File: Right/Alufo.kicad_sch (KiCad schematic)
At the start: 23 parts, among them J2 USB_C_Receptacle_USB2.0_16P_2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, J4 USB_C_Receptacle_USB2.0_16P_2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, SW2 BOOT, U2 CH552T, U4 USBLC6-2P6, U6 USBLC6-2P6

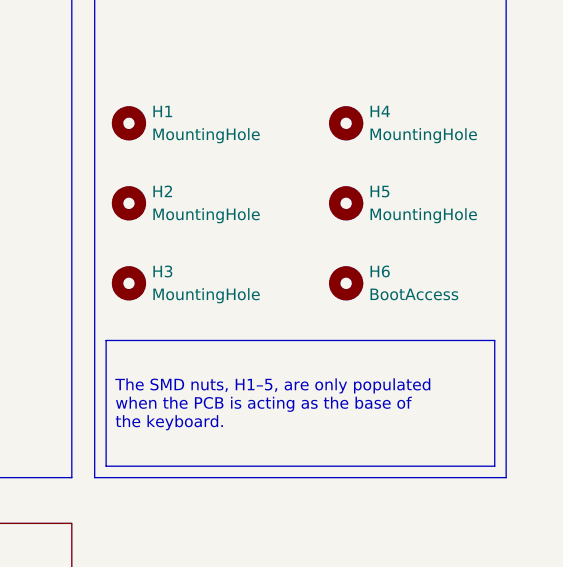
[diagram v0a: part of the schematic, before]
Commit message: Revert boot access hole change
It was correct before!
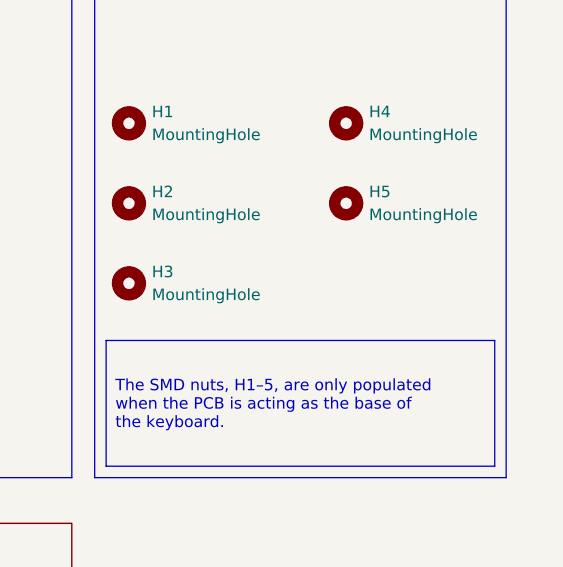
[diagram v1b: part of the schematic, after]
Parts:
- removed H6: BootAccess, MountingHole:MountingHole_2.5mm, symbol Mechanical:MountingHole
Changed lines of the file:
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@@
-	)
-	(symbol
-		(lib_id "Mechanical:MountingHole")
-		(at 177.8 176.53 0)
-		(unit 1)
-		(exclude_from_sim yes)
-		(in_bom no)
-		(on_board yes)
-		(dnp no)
-		(fields_autoplaced yes)
-		(property "Reference" "H6"
-			(at 180.34 175.2599 0)
-			(effects
-				(font
-					(size 1.27 1.27)
-				)
-				(justify left)
-			)
-		)
-		(property "Value" "BootAccess"
-			(at 180.34 177.7999 0)
-			(effects
-				(font
-					(size 1.27 1.27)
-				)
-				(justify left)
-			)
-		)
-		(property "Footprint" "MountingHole:MountingHole_2.5mm"
-			(at 177.8 176.53 0)
-			(effects
-				(font
-					(size 1.27 1.27)
-				)
-				(hide yes)
-			)
-		)
-		(property "Datasheet" "~"
-			(at 177.8 176.53 0)
-			(effects
-				(font
-					(size 1.27 1.27)
-				)
-				(hide yes)
-			)
-		)
-		(property "Description" "Mounting Hole without connection"
-			(at 177.8 176.53 0)
-			(effects
-				(font
-					(size 1.27 1.27)
-				)
-				(hide yes)
-			)
-		)
-		(instances
-			(project "Alufo"
-				(path "/52f043ac-ccff-4c85-bc10-2db9d3c9e3f3"
-					(reference "H6")
-					(unit 1)
-				)
-			)
-		)
 	)
 	(symbol

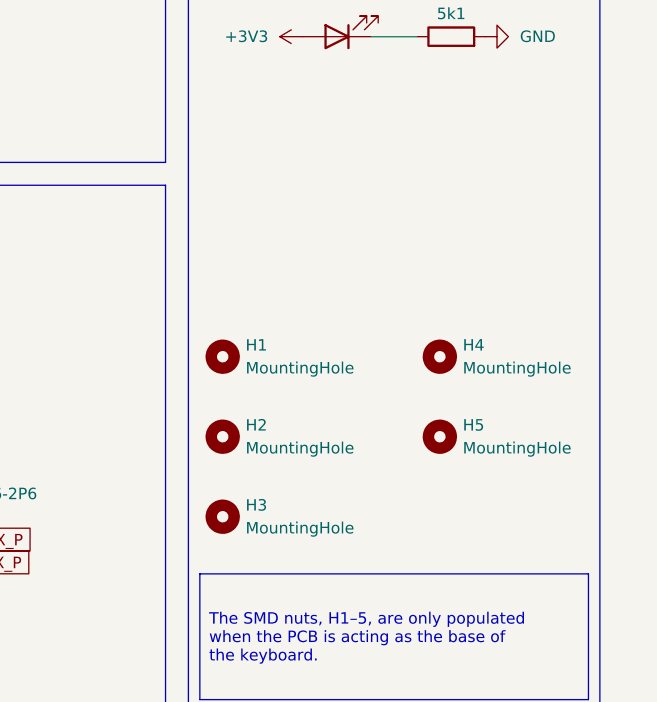
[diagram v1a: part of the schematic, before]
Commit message: Add plate to righthand board
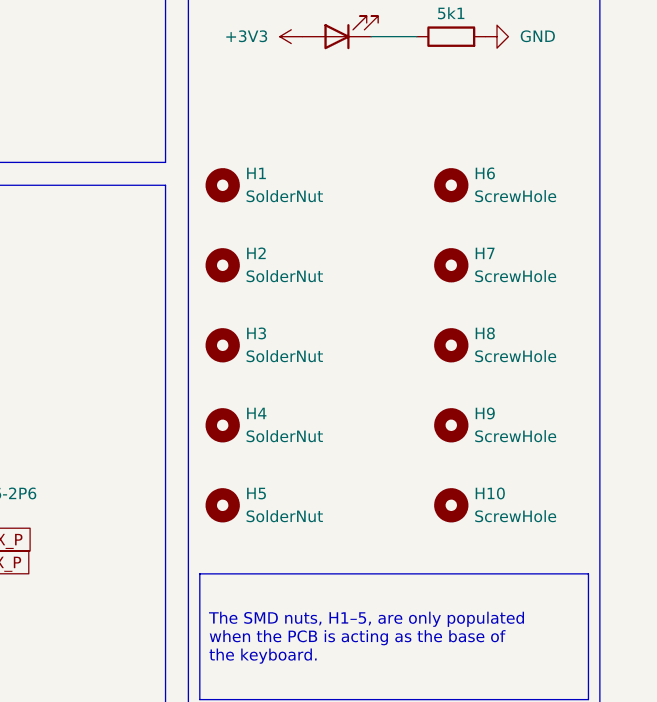
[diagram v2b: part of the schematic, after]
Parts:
- added H10, H6, H7, H8, H9: ScrewHole, MountingHole:MountingHole_2.2mm_M2, symbol Mechanical:MountingHole
- H1, H2, H3, H4, H5: value MountingHole -> SolderNut

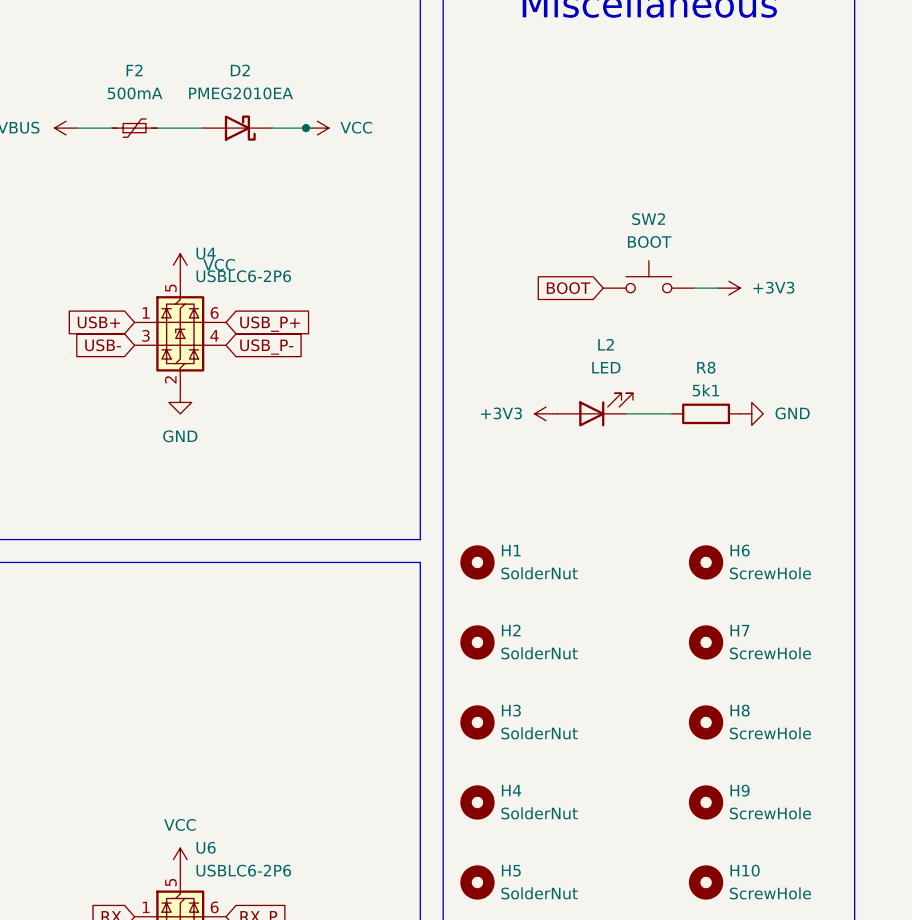
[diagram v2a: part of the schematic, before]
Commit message: Connect aluminium back to copper layer
Holes J5 and J6 will be filled with solder on the active PCB to connect the back aluminium layer (which is connected to the USB shield) with the mounting hole H3. H3 will in turn connect to the bottom layer PCB via the solder nut pressed against the exposed pad on the active PCB. The solder nut will connect to the screw and the screw will connect to the top plate. The upper middle plate will connect to the shield by virtue of being physically pressed to the active PCB’s back (if correctly oriented).
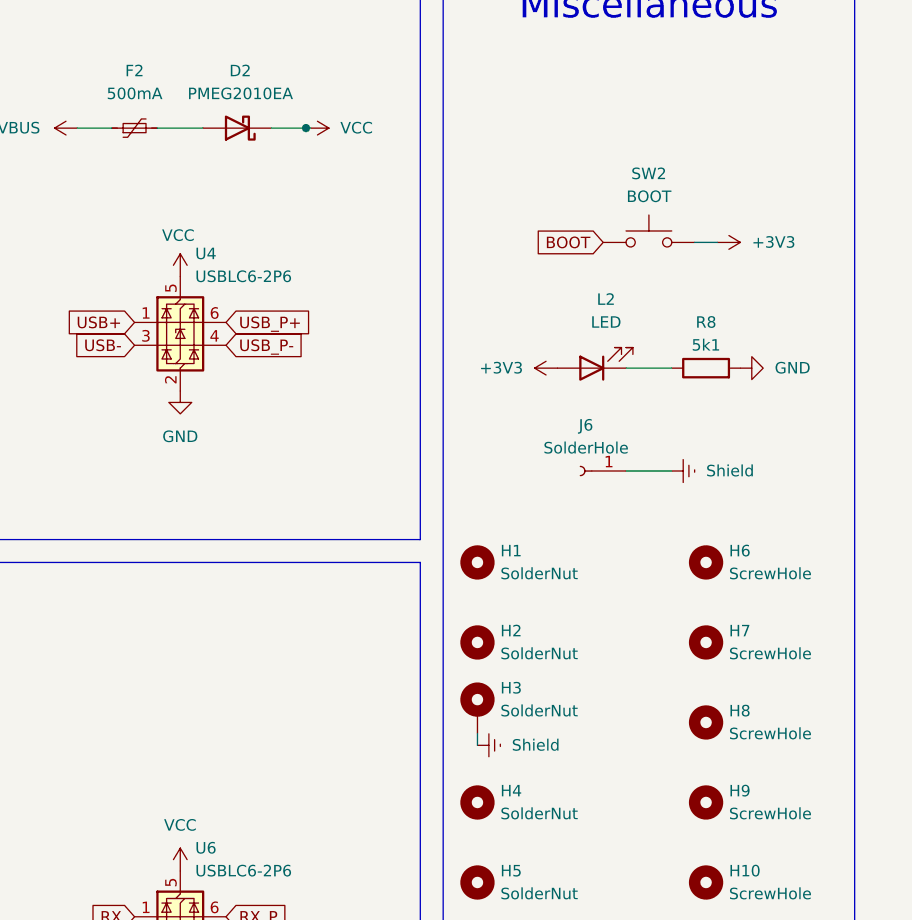
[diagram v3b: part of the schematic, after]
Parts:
- added J6: SolderHole, TestPoint:TestPoint_THTPad_D2.5mm_Drill1.2mm, symbol Connector:Conn_01x01_Socket
- H3: footprint Project Library:MountingHole_2.2mm_M2_SMD_Solder_Nut -> Project Library:MountingHole_2.2mm_M2_SMD_Solder_Nut_Pad; symbol Mechanical:MountingHole -> Mechanical:MountingHole_Pad
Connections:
- new net Shield: H3.1, J6.1 (Pin_1)
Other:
- moved on the sheet: L2, R8, SW2

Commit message: Do not exclude solder nuts from BOM
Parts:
- H1, H2, H3, H4, H5: now in the parts list

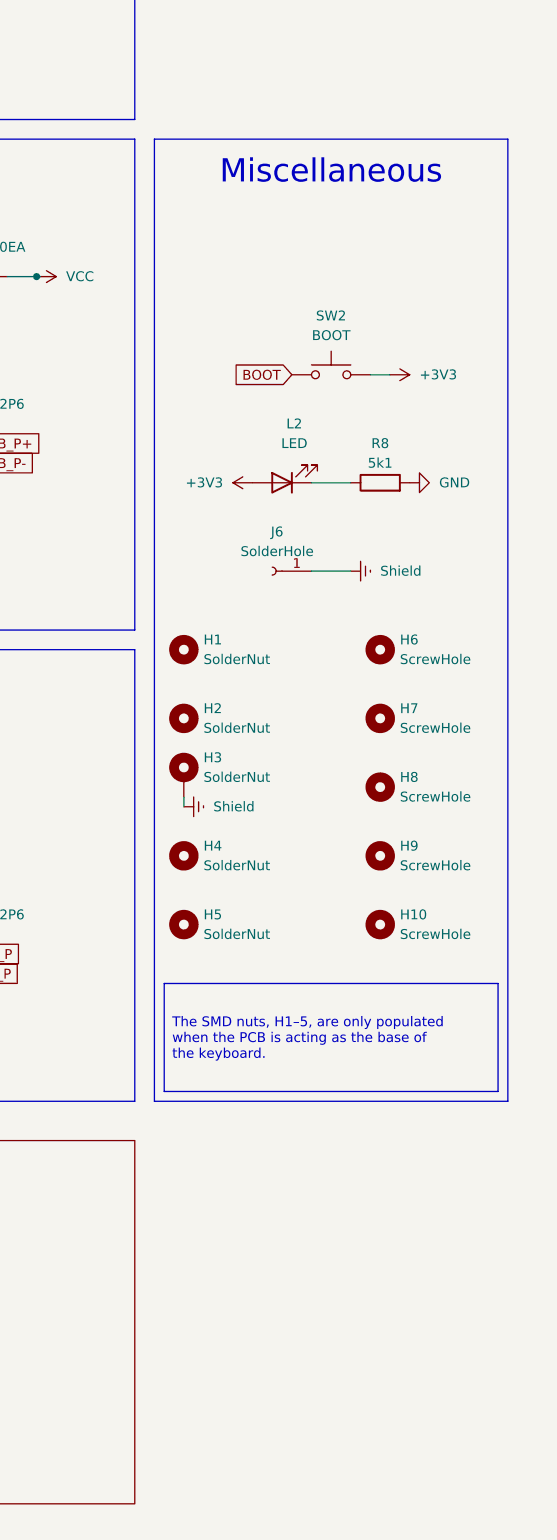
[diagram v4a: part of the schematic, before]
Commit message: Update link between PCB and plate
There are now two connections, with mouse bites at both ends.
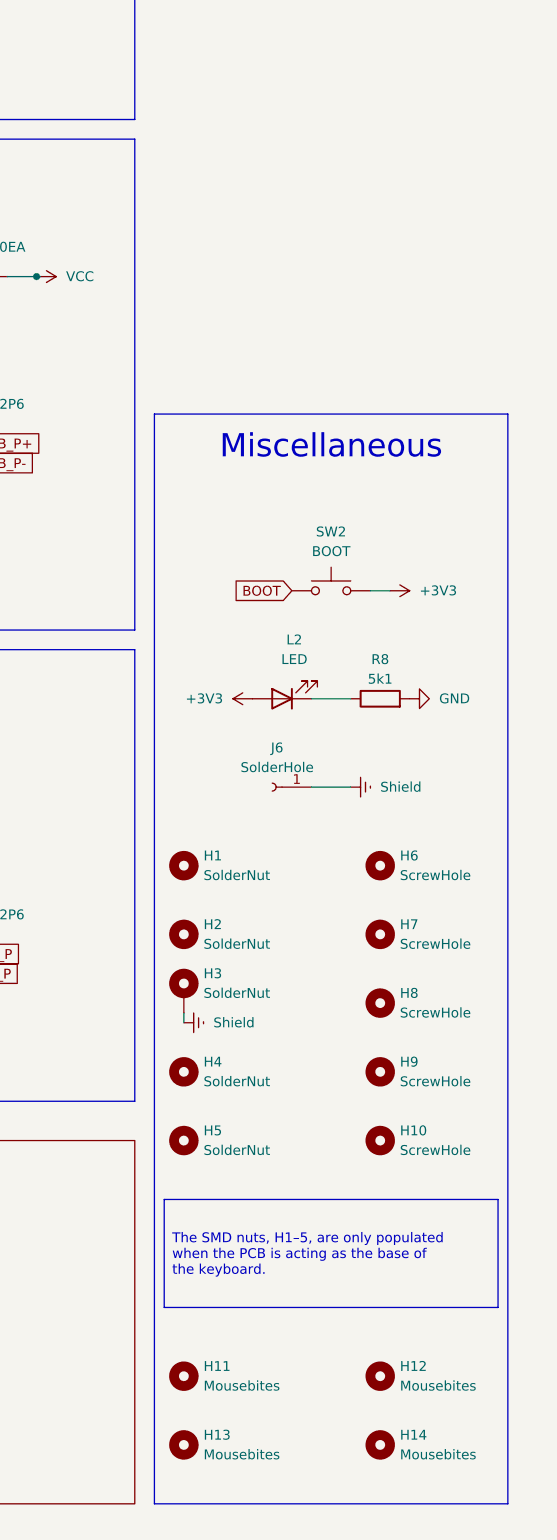
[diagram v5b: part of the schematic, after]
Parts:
- added H11, H12, H13, H14: Mousebites, Project Library:Mousebites, symbol Mechanical:MountingHole
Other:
- moved on the sheet: H1, H10, H2, H3, H4, H5, H6, H7, H8, H9, J6, L2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
